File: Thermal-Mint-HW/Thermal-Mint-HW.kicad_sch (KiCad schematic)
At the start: 12 parts

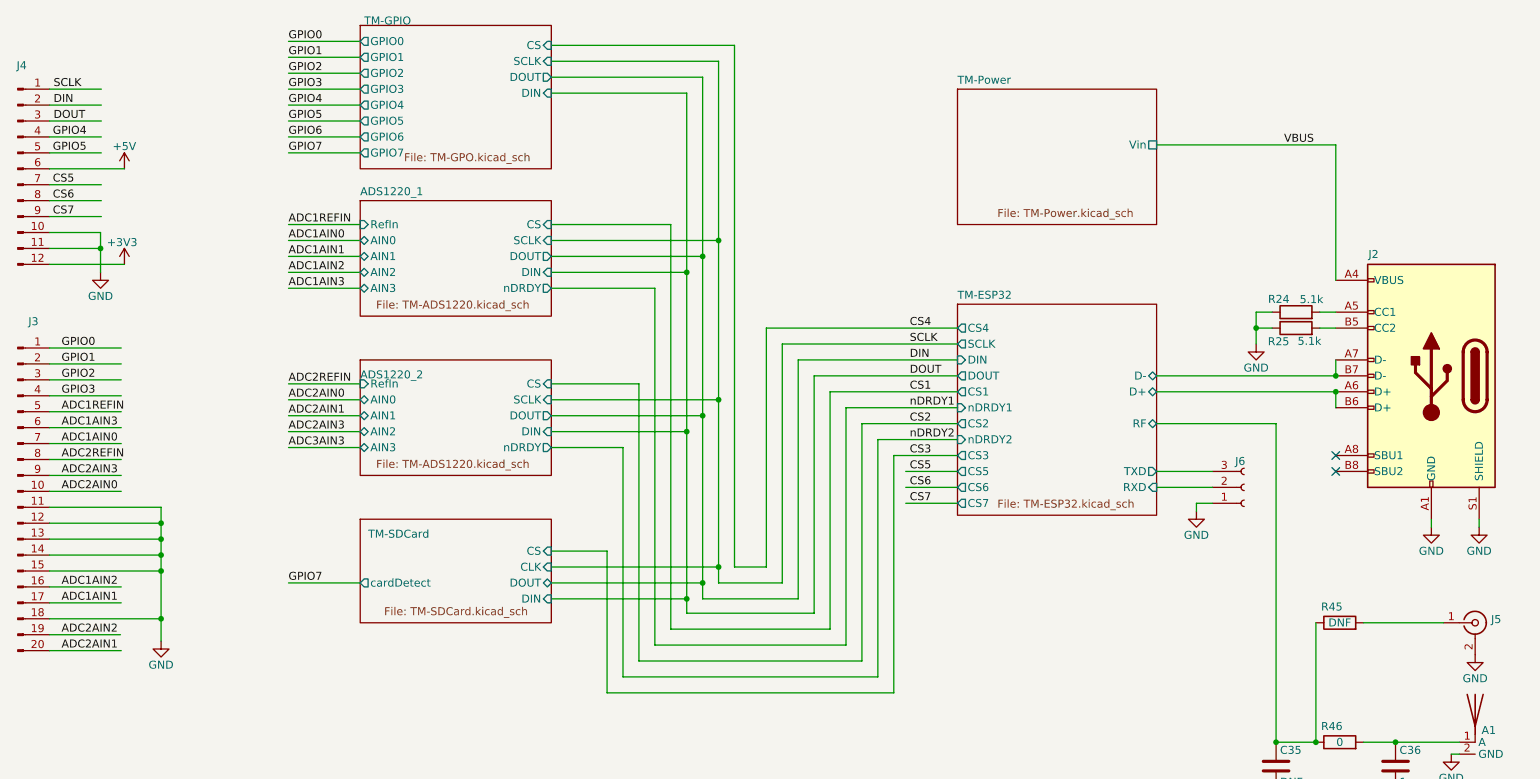
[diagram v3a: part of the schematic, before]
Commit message: Temporary commit before changing processor from C3 to s2
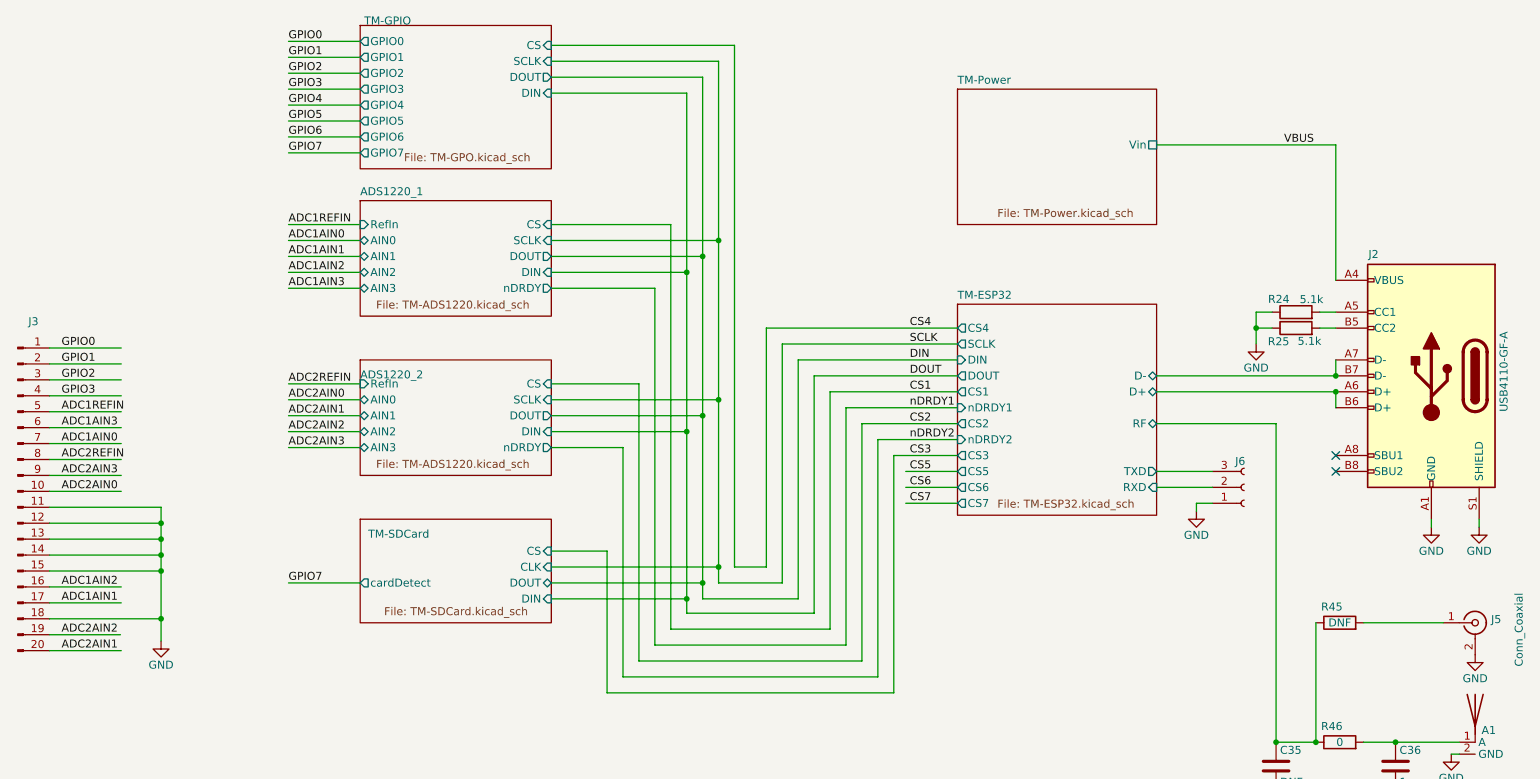
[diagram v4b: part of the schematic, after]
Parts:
- removed J4: (no value), symbol Connector:Conn_01x12_Male
- A1: value (none) -> AntennaWithGround; footprint (none) -> ThermalMint:WifiAntenna
- J2: value (none) -> USB4110-GF-A; footprint (none) -> ThermalMint:USB4110-GF-A
- J3: value (none) -> Conn_01x20_Male
- J5: value (none) -> Conn_Coaxial; footprint (none) -> Connector_Coaxial:SMA_Amphenol_132289_EdgeMount
- J6: value (none) -> Conn_01x03_Female; footprint (none) -> Connector_PinHeader_2.54mm:PinHeader_1x03_P2.54mm_Vertical

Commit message: Schematic update to ESP32-S2
Updated schematic from ESP32-C3 to the S2 chips with more pins, allowed the removal of the GPO expander and CS mux as well as addition of JTAG
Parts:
- removed J6: Conn_01x03_Female, Connector_PinHeader_2.54mm:PinHeader_1x03_P2.54mm_Vertical, symbol Connector:Conn_01x03_Female
- added C1 (x2), C2 (x2), C4 (x2), C6 (x2): 10n, Capacitor_SMD:C_0603_1608Metric_Pad1.08x0.95mm_HandSolder, symbol Device:C
- added C17, C19 (x3), C24 (x5), C8 (x2): 100n, Capacitor_SMD:C_0603_1608Metric_Pad1.08x0.95mm_HandSolder, symbol Device:C
- added C18 (x2), C28, C30, C7 (x2): 1u, Capacitor_SMD:C_0603_1608Metric_Pad1.08x0.95mm_HandSolder, symbol Device:C
- added C19: 0.1n, Capacitor_SMD:C_0603_1608Metric_Pad1.08x0.95mm_HandSolder, symbol Device:C
- added C25: 0.5p, Capacitor_SMD:C_0603_1608Metric_Pad1.08x0.95mm_HandSolder, symbol Device:C
- added C25, C29, C3 (x2), C31, C34, C5 (x2): 470n, Capacitor_SMD:C_0603_1608Metric_Pad1.08x0.95mm_HandSolder, symbol Device:C
- added C26, C27: 15p, Capacitor_SMD:C_0603_1608Metric_Pad1.08x0.95mm_HandSolder, symbol Device:C
- added C37, C38: DNF, Capacitor_SMD:C_0603_1608Metric_Pad1.08x0.95mm_HandSolder, symbol Device:C
- added D1, D2, D3, D4: LED, symbol Device:LED
- added J1: Molex_5031821852, ThermalMint:Molex_SDCard_5031821852, symbol ThermalMint:Molex_5031821852
- added J1: Conn_01x07_Pin, symbol Connector:Conn_01x07_Pin
- added L1: 2n, symbol Device:L
- added L2: 6.8n, symbol Device:L
- added Q1, Q3, Q5, Q7: PNP, symbol Simulation_SPICE:PNP
- added Q2, Q4, Q6, Q8: NPN, symbol Simulation_SPICE:NPN
- added R1 (x2), R2 (x2), R47: DNF, Resistor_SMD:R_0603_1608Metric_Pad0.98x0.95mm_HandSolder, symbol Device:R
- added R1: 0, Resistor_SMD:R_0603_1608Metric_Pad0.98x0.95mm_HandSolder, symbol Device:R
- added R17, R23, R32: 10k, Resistor_SMD:R_0603_1608Metric_Pad0.98x0.95mm_HandSolder, symbol Device:R
- added R18 (x2), R19 (x6), R22, R26, R27, R28, R29, R30: 24, Resistor_SMD:R_0603_1608Metric_Pad0.98x0.95mm_HandSolder, symbol Device:R
- added R19 (x4), R27 (x4): 1k, Resistor_SMD:R_0603_1608Metric_Pad0.98x0.95mm_HandSolder, symbol Device:R
- added R19 (x4): 15k, Resistor_SMD:R_0603_1608Metric_Pad0.98x0.95mm_HandSolder, symbol Device:R
- added R3 (x2), R4 (x2), R5 (x2), R7 (x2): 820, Resistor_SMD:R_0603_1608Metric_Pad0.98x0.95mm_HandSolder, symbol Device:R
- added R6 (x2): 1.65k, Resistor_SMD:R_0603_1608Metric_Pad0.98x0.95mm_HandSolder, symbol Device:R
- added R8 (x2): 10, Resistor_SMD:R_0603_1608Metric_Pad0.98x0.95mm_HandSolder, symbol Device:R
- added SW1, SW2: PTS647, ThermalMint:SW_SPST_PTS647, symbol ThermalMint:PTS647
- added U1: ~, symbol ThermalMint:ESP32-S2
- added U1 (x2): ADS1220-VQFN, CH:QFN-16_EP_3.5x3.5_Pitch0.5mm, symbol NoSim:ADS1220-VQFN
- added U4: AT25DL081-SSHN-T, Package_SO:SOIC-8_3.9x4.9mm_P1.27mm, symbol ThermalMint:AT25DL081-SSHN-T
- added U5: NCP1117-3.3_SOT223, Package_TO_SOT_SMD:SOT-223-3_TabPin2, symbol Regulator_Linear:NCP1117-3.3_SOT223
- added Y1: FL4000157Z, Crystal:Crystal_SMD_3225-4Pin_3.2x2.5mm, symbol Device:Crystal_GND24
- added Y2: CM8V-T1A-32.768KHZ-12.5PF-20PPM-TA-QA, Crystal:Crystal_SMD_TXC_9HT11-2Pin_2.0x1.2mm_HandSoldering, symbol Device:Crystal
- C35: value DNF -> 0.5p
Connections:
- net ADC1AIN0: now also R1.2, R3.1
- net ADC1AIN1: now also R2.1, R4.1
- net ADC1AIN2: now also U1.5 (AIN2)
- net ADC1AIN3: now also U1.4 (AIN3/REFN1)
- net ADC1REFIN: now also R5.1, R6.1
- net ADC2AIN0: now also R1.2, R3.1
- net ADC2AIN1: now also R2.1, R4.1
- net ADC2AIN2: now also U1.5 (AIN2)
- net ADC2AIN3: now also U1.4 (AIN3/REFN1)
- net ADC2REFIN: now also R5.1, R6.1
- net GND: now also C1.1, C1.1, C17.2, C18.2, C18.2, C19.2, C19.2, C19.2, C19.2, C2.2, C2.2, C24.2, C24.2, C24.2, C24.2, C24.2, C25.2, C25.2, C26.2, C27.2, C28.2, C29.2, C30.2, C31.2, C34.2, C37.2, C38.2, C4.2, C4.2, C6.1, C6.1, C7.2, C7.2, C8.2, C8.2, D1.1 (K), D2.1 (K), D3.1 (K), D4.1 (K), J1.10 (SW_Shield), J1.11 (Shield), J1.12 (Shield), J1.13 (Shield), J1.14 (Shield), J1.15 (Shield), J1.6 (VSS), J1.7 (Pin_7), R19.2, R19.2, R19.2, R19.2, R19.2, R19.2, R19.2, R19.2, R2.2, R2.2, R32.2, R6.2, R6.2, R7.1, R7.1, SW1.3, SW1.4, SW2.3, SW2.4, U1.1 (CLK), U1.1 (CLK), U1.17 (EP), U1.17 (EP), U1.2 (DGND), U1.2 (DGND), U1.3 (AVSS), U1.3 (AVSS), U1.57 (GND), U4.4 (GND), U5.1 (GND), Y1.2, Y1.4
- net GPIO0 renamed xGPO1
- net xGPO1: now also R19.1
- net GPIO1 renamed xGPO2
- net xGPO2: now also R19.1
- net GPIO2 renamed xGPO3
- net xGPO3: now also R19.1
- net GPIO3 renamed xGPO4
- net xGPO4: now also R19.1
- net TM-ESP32/D+ renamed USBD_P
- net USBD_P: now also U1.26 (GPIO20)
- net TM-ESP32/D- renamed USBD_N
- net USBD_N: now also U1.25 (GPIO19)
- net TM-ESP32/RF: no longer names the net of C35.1, R45.1, R46.1
- net TM-ESP32/RF: now also L2.1
- net VBUS renamed +5V
- net +5V: now also C28.1, C29.1, Q1.3 (E), Q3.3 (E), Q5.3 (E), Q7.3 (E), U5.3 (VI)
- new net: C4.1, C5.2, R5.2, U1.7 (REFP0) (x2)
- new net: R27.1, U1.40 (GPIO36)
- new net: D1.2 (A), R27.2
- new net: D2.2 (A), R27.2
- new net: C24.1, L1.2, U1.3 (VDD3P3), U1.4 (VDD3P3)
- new net: Q5.2 (B), Q6.1 (C)
- new net: Q6.3 (E), R19.1
- new net: C5.1, C6.2, R7.2, U1.6 (REFN0) (x2)
- new net: C1.2, C3.1, R3.2, U1.9 (AIN0/REFP1) (x2)
- new net: C7.1, R8.1, U1.10 (AVDD) (x2)
- new net: Q1.1 (C), R19.2
- new net: Q3.1 (C), R19.2
- new net: C2.1, C3.2, R4.2, U1.8 (AIN1) (x2)
- new net: Q1.2 (B), Q2.1 (C)
- new net: C26.1, R1.2, Y1.1
- new net: Q3.2 (B), Q4.1 (C)
- new net: Q4.3 (E), R19.1
- new net: Q8.3 (E), R19.1
- new net: J1.7 (DAT0), R22.1
- new net: Q7.1 (C), R19.2
- new net: Q7.2 (B), Q8.1 (C)
- new net: R29.1, U4.2 (DO)
- new net: R30.1, U4.3 (/WP)
- new net: R28.1, U4.5 (DI)
- new net: R26.2, U4.6 (CLK)
- new net: R27.2, U4.7 (/HOLD)
- new net: R27.1, U1.39 (GPIO35)
- new net: R27.1, U1.41 (GPIO37)
- new net: R27.1, U1.42 (GPIO38)
- new net: J1.6 (Pin_6), U1.43 (MTCK)
- new net: J1.5 (Pin_5), U1.44 (MTDO)
- new net: J1.4 (Pin_4), U1.46 (MTDI)
- new net: J1.3 (Pin_3), U1.47 (MTMS)
- new net: J1.2 (Pin_2), U1.48 (U0TXD)
- new net: J1.1 (Pin_1), U1.49 (U0RXD)
- new net: R32.1, U1.55 (GPIO46)
- new net: D4.2 (A), R27.2
- new net: Q5.1 (C), R19.2
- new net: R19.1, U1.12 (nDRDY) (x2)
- new net: R18.1, U1.13 (DOUT/nDRDY) (x2)
- new net: Q2.3 (E), R19.1
- new net: D3.2 (A), R27.2
- new net +3V3: C18.1, C18.1, C19.1, C19.1, C19.1, C19.1, C24.1, C24.1, C24.1, C24.1, C30.1, C31.1, C34.1, C8.1, C8.1, J1.4 (VDD), L1.1, R17.1, R23.1, R8.2, R8.2, U1.1 (VDDA), U1.11 (DVDD), U1.11 (DVDD), U1.20 (VDD3P3_RTC), U1.27 (VDD3P3_RTC_IO), U1.30 (VDD_SPI), U1.45 (VDD3P3_CPU), U1.51 (VDDA), U1.54 (VDDA), U4.8 (VCC), U5.2 (VO)
- new net ADC1_CS: U1.16 (nCS), U1.6 (GPIO1)
- new net ADC1_DRDY: R19.2, U1.9 (GPIO4)
- new net ADC2_CS: U1.16 (nCS), U1.7 (GPIO2)
- new net ADC2_DRDY: R19.2, U1.10 (GPIO5)
- new net AVDD: R1.1, R1.1
- new net BOOT_SEL: SW1.1, SW1.2, U1.5 (GPIO0)
- new net CHIP_PU: C25.1, R17.2, SW2.1, SW2.2, U1.56 (CHIP_PU)
- new net GPO1: Q8.2 (B), R19.1, U1.15 (GPIO10)
- new net GPO2: Q6.2 (B), R19.1, U1.16 (GPIO11)
- new net GPO3: Q4.2 (B), R19.1, U1.17 (GPIO12)
- new net GPO4: Q2.2 (B), R19.1, U1.18 (GPIO13)
- new net RF: C25.1, L2.2, U1.2 (LNA_IN)
- new net SD_CS: J1.2 (DAT3/CD), U1.8 (GPIO3)
- new net SD_CardDetect: J1.9 (SW), R23.2, U1.11 (GPIO6)
- new net SPICLK: R26.1, U1.34 (SPICLK)
- new net SPICS0: U1.33 (SPICS0), U4.1 (/CS)
- new net SPID: R28.2, U1.36 (SPID)
- new net SPIHD: R27.1, U1.31 (SPIHD)
- new net SPIQ: R29.2, U1.35 (SPIQ)
- new net SPIWP: R30.2, U1.32 (SPIWP)
- new net SPI_CLK: J1.5 (CLK), U1.12 (GPIO7), U1.15 (SCLK), U1.15 (SCLK)
- new net SPI_DIN: R18.2, R18.2, R22.2, U1.14 (GPIO9)
- new net SPI_DOUT: J1.3 (CMD), U1.13 (GPIO8), U1.14 (DIN), U1.14 (DIN)
- new net XTAL_32k_N: C38.1, R47.1, U1.22 (XTAL_32K_N), Y2.1
- new net XTAL_32k_P: C37.1, R47.2, U1.21 (XTAL_32K_P), Y2.2
- new net XTAL_N: C27.1, U1.52 (XTAL_N), Y1.3
- new net XTAL_P: R1.1, U1.53 (XTAL_P)
- no-connect marks 2 -> 4
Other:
- removed sheet ADS1220_1
- removed sheet ADS1220_2
- removed sheet TM-ESP32
- removed sheet TM-GPIO
- removed sheet TM-Power
- removed sheet TM-SDCard
- note added: "50 Ohm Single Ended Impedance"
- note added: "90 Ohm Differential Impedance"
- moved on the sheet: A1, C35, C36, J2, J3, J5, R24, R25, R45, R46
